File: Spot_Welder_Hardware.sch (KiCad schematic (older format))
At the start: 141 parts

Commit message: modified component values
Final touchups before schematic review.
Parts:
- removed C?: 10uF, symbol C
- removed D?: D, symbol D
- removed D?: 5V, symbol D_Zener
- removed D?: 9V, symbol D_Zener
- removed D?: Over Voltage, symbol LED
- removed Q?: Q_PMOS_GDSD, symbol Q_PMOS_GDSD
- removed R?: 1500, symbol R
- removed R? (x2): 1000, symbol R
- removed U?: FAN3121TMXCT-ND, symbol FAN3122TMXCT-ND
- added C?: 47mF, symbol CP1
- added D?: Over Voltage, symbol LED
- added D?: 20V, symbol D_Schottky
- added R? (x2): 5, symbol R
- added R?: 250, symbol R
- R?: value 10k -> 5; Part Number (none) -> YAG1224CT-ND
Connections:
- wire segments 161 -> 144
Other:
- note added: "30 parallel capacitors @4700uF and 14mOhm ESR \n yields 1.41F and .47mOhm ESR"
- note added: "Active Low\n"
- note added: "Ideas: Zener diode\n OpAmp with Zener control"
- note added: "Safety Short VS to Ground"
- note added: "ToDo: Find capacitance"
- note added: "at 15Ohm and 1.4F, t = 10s\n 5t = 50s\nAt 15V, each resistor will carry 5W"
- note added: "main constraints: Output current requirement \n to effectively charge 1.41F\n LED Indication"
- note removed: "ToDo: Find reason and capacitance"
- note removed: "ToDo:\nWhat Cap value to use \nto combat brownout"
- moved on the sheet: R?, SW?

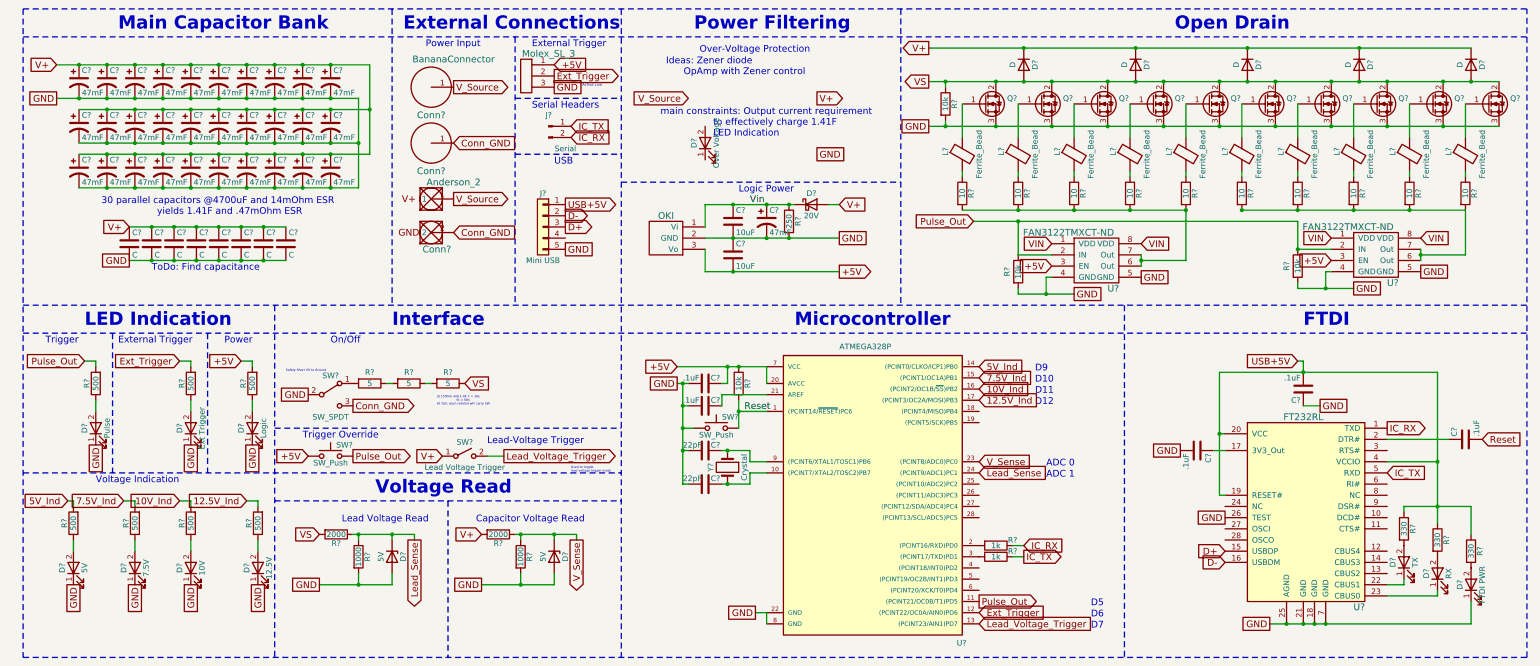
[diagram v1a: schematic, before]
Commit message: Added Buzzer circuitry
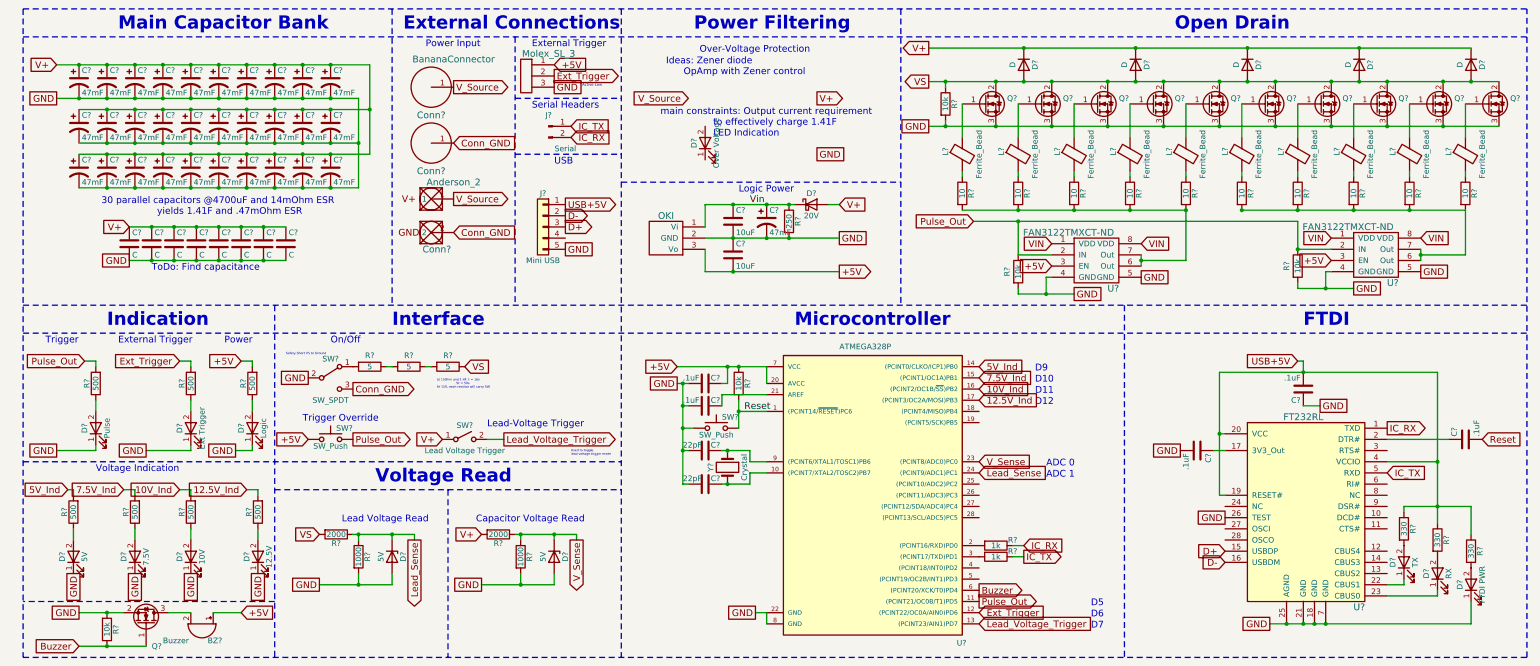
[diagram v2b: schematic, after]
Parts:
- added BZ?: Buzzer, symbol Buzzer
- added Q?: Q_NMOS_GSD, symbol Q_NMOS_GSD
- added R?: 10k, symbol R
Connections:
- net +5V: now also BZ?.1 (-)
- net GND: now also Q?.2 (S), R?.2
- net Buzzer: now reaches U?.6 ((PCINT20/XCK/T0)PD4)
- net Buzzer: now also Q?.1 (G), R?.1
- new net: BZ?.2 (+), Q?.3 (D)
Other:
- note added: "Indication"
- note removed: "LED Indication"
- moved on the sheet: D?, R?, SW?

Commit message: Added Buzzer Part number
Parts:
- BZ?: Part Number (none) -> 668-1336-1-ND
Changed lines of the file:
@@
 F 2 "" V 3425 7500 50  0001 C CNN
 F 3 "" V 3425 7500 50  0001 C CNN
+F 4 "668-1336-1-ND" V 3450 7400 60  0001 C CNN "Part Number"
 	1    3450 7400
 	0    1    1    0
